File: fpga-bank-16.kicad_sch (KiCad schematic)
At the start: 3 parts, among them U4 XC7K160T-FFG676

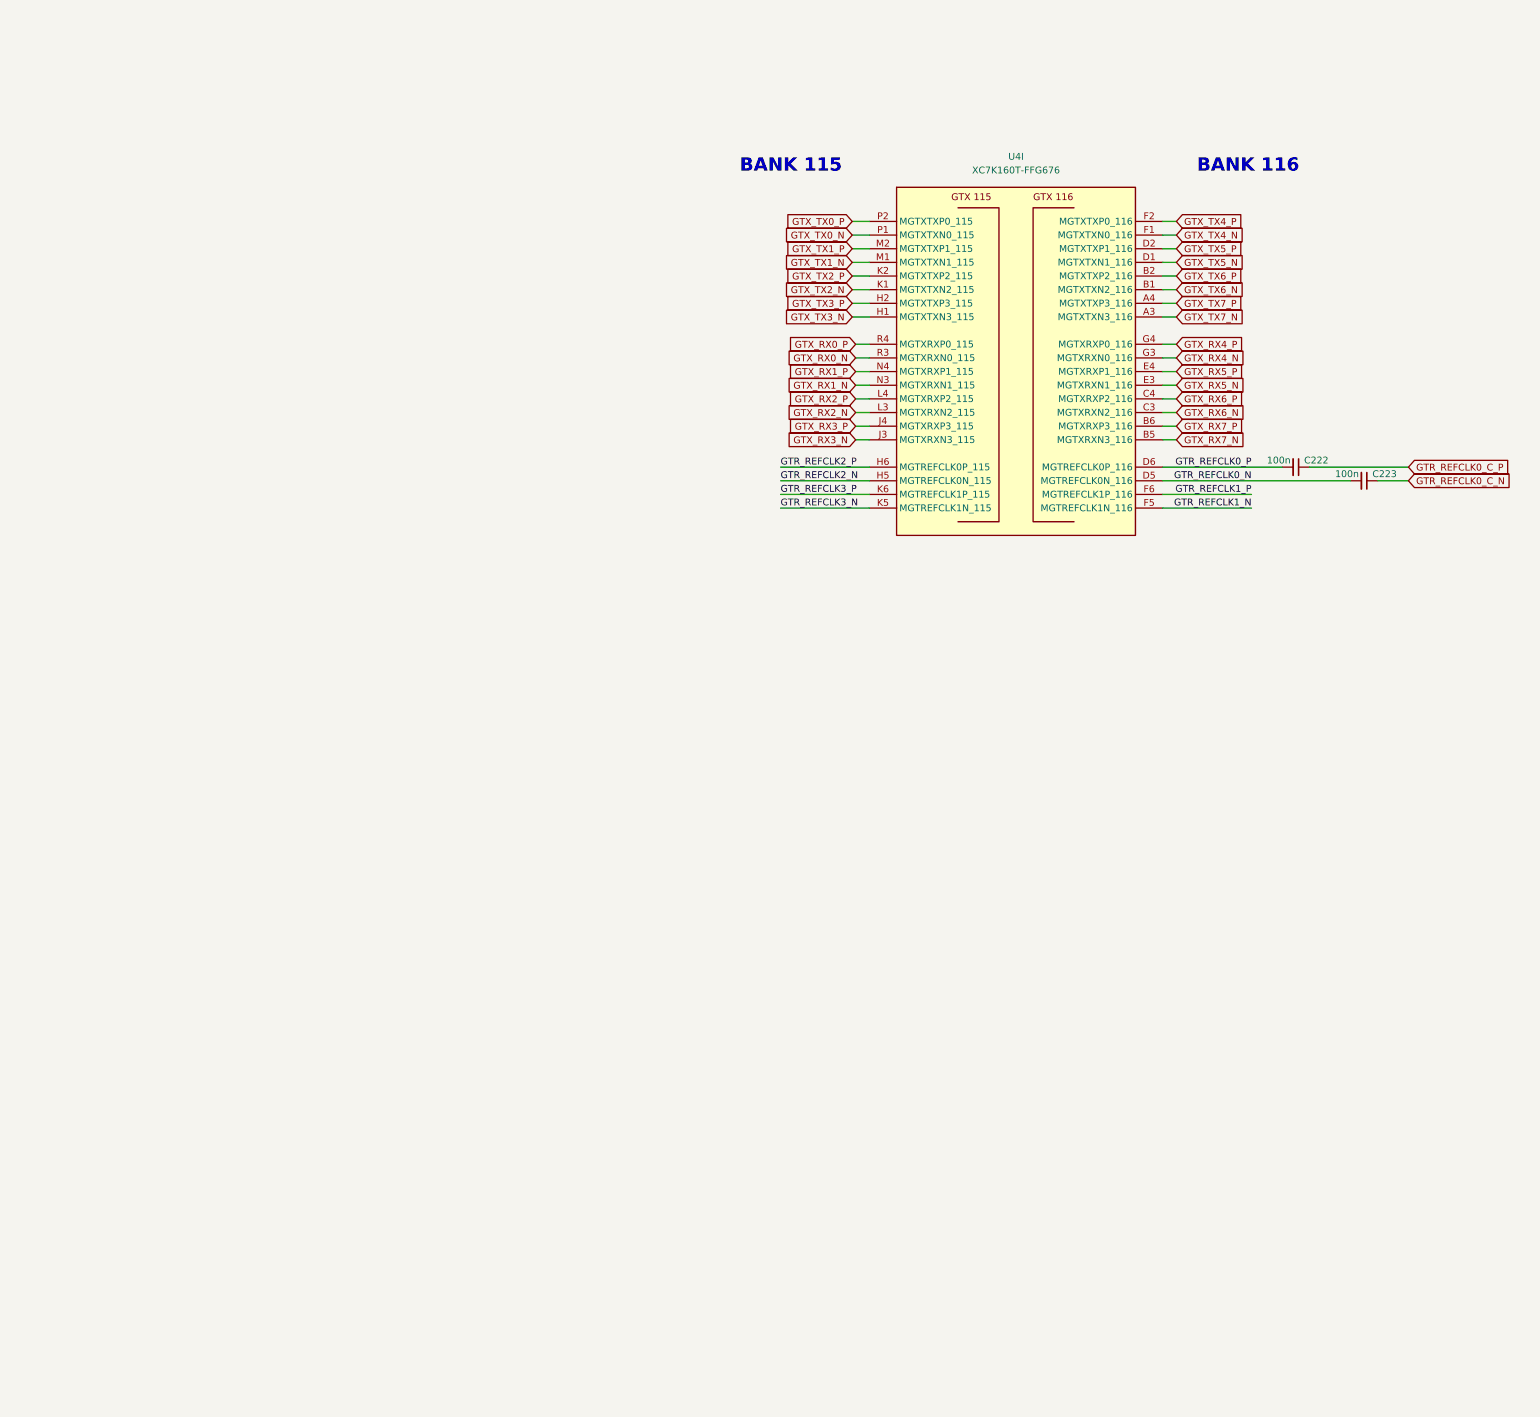
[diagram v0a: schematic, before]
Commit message: Finish creating hierarchical buses and structure, start reconnecting signals
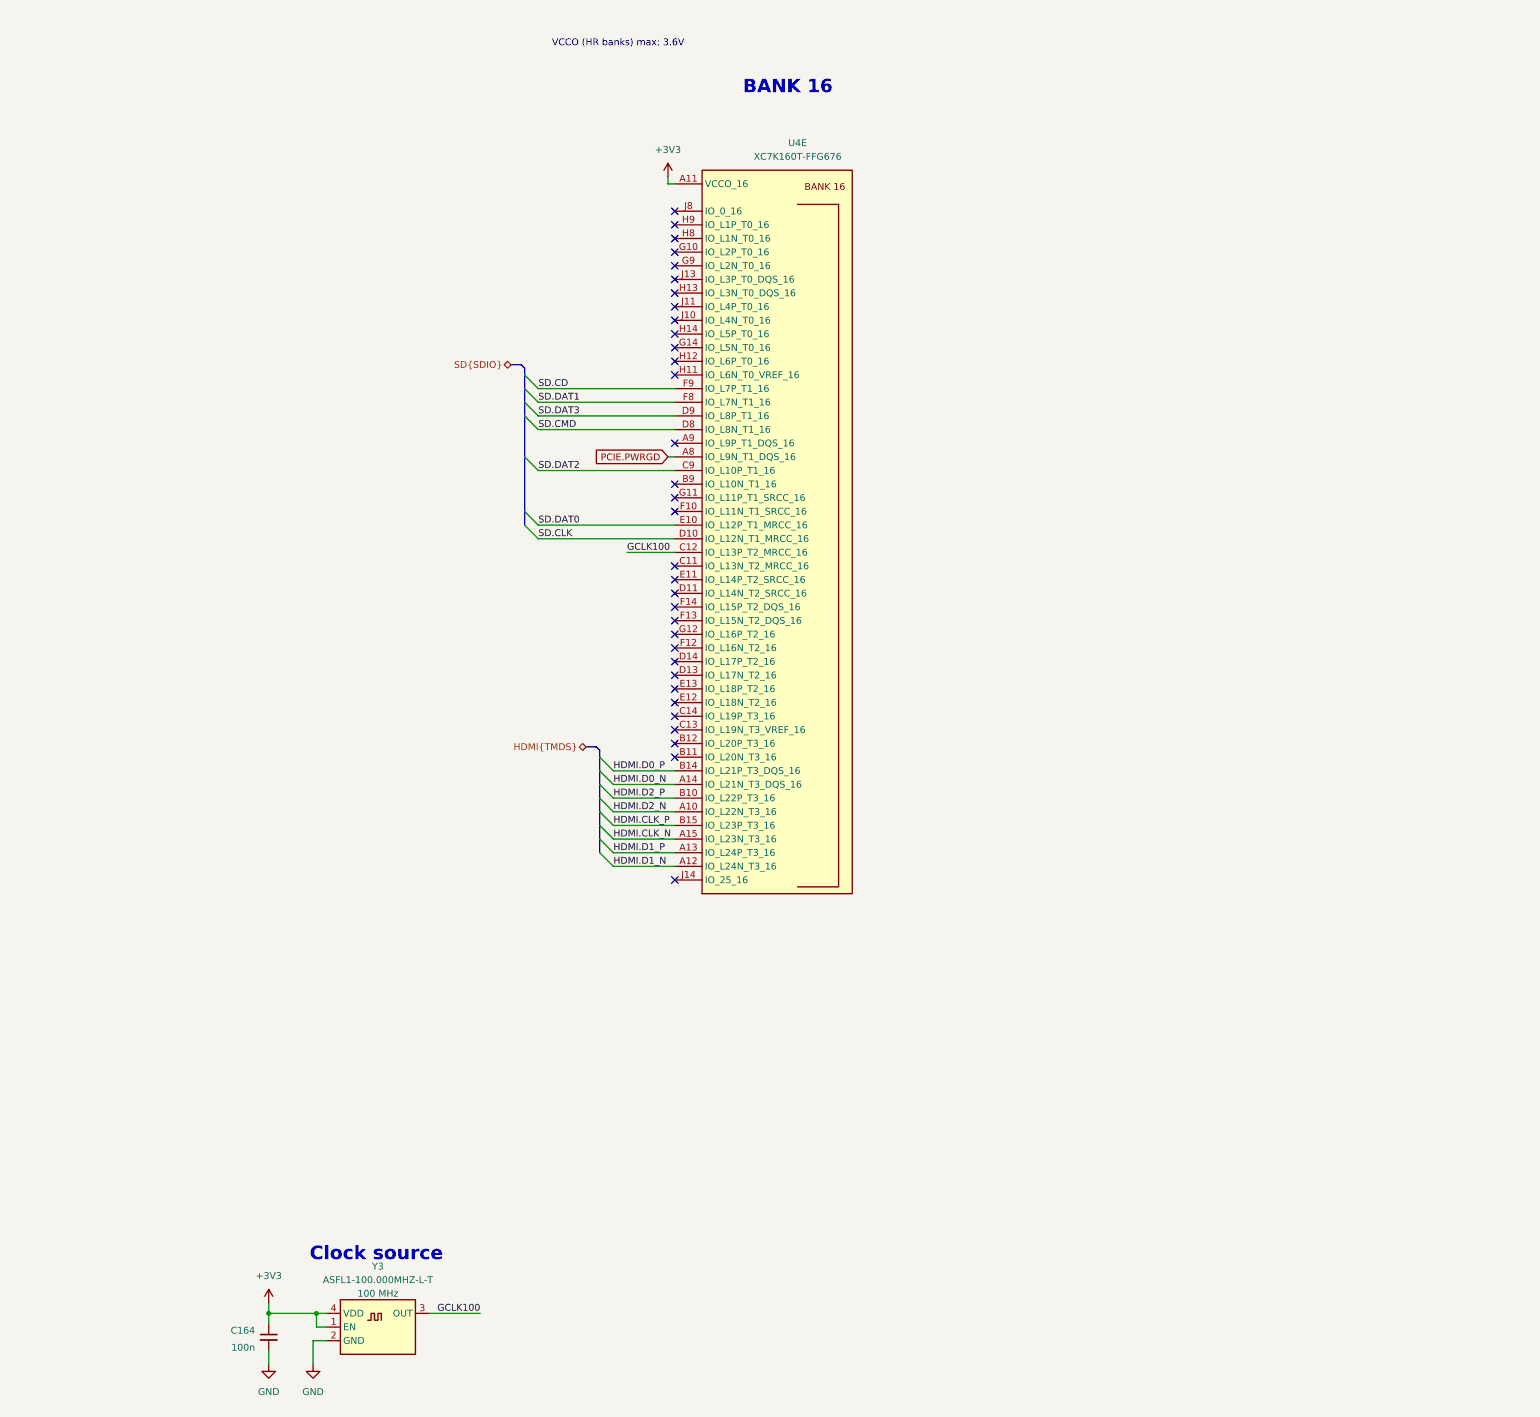
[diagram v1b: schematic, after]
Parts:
- removed C222, C223: C_100n_0402, sodimm-ddr5-tester-footprints:C_0402_1005Metric, symbol sodimm-ddr5-tester:C_100n_0402
- removed U4: XC7K160T-FFG676, sodimm-ddr5-tester-footprints:BGA-676_27x27mm_Layout26x26_P1X1mm, symbol sodimm-ddr5-tester:XC7K160T-FFG676
- added C164: C_100n_0402, sodimm-ddr5-tester-footprints:C_0402_1005Metric, symbol sodimm-ddr5-tester:C_100n_0402
- added U4: XC7K160T-FFG676, sodimm-ddr5-tester-footprints:BGA-676_27x27mm_Layout26x26_P1X1mm, symbol sodimm-ddr5-tester:XC7K160T-FFG676
- added Y3: Oscillator_100MHz_ASFL1, sodimm-ddr5-tester-footprints:Oscillator_SMD_Abracon_ASFL1-4Pin_5.0x3.2mm, symbol sodimm-ddr5-tester:Oscillator_100MHz_ASFL1
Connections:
- new net +3V3: C164.1, U4.A11 (VCCO_16), U4.B8 (VCCO_16), U4.C15 (VCCO_16), U4.D12 (VCCO_16), U4.E9 (VCCO_16), U4.G13 (VCCO_16), U4.H10 (VCCO_16), Y3.1 (EN), Y3.4 (VDD)
- new net GCLK100: U4.C12 (IO_L13P_T2_MRCC_16), Y3.3 (OUT)
- new net GND: C164.2, Y3.2 (GND)
- new net HDMI.CLK_N: U4.A15 (IO_L23N_T3_16)
- new net HDMI.CLK_P: U4.B15 (IO_L23P_T3_16)
- new net HDMI.D0_N: U4.A14 (IO_L21N_T3_DQS_16)
- new net HDMI.D0_P: U4.B14 (IO_L21P_T3_DQS_16)
- new net HDMI.D1_N: U4.A12 (IO_L24N_T3_16)
- new net HDMI.D1_P: U4.A13 (IO_L24P_T3_16)
- new net HDMI.D2_N: U4.A10 (IO_L22N_T3_16)
- new net HDMI.D2_P: U4.B10 (IO_L22P_T3_16)
- new net PCIE.PWRGD: U4.A8 (IO_L9N_T1_DQS_16)
- new net SD.CD: U4.F9 (IO_L7P_T1_16)
- new net SD.CLK: U4.D10 (IO_L12N_T1_MRCC_16)
- new net SD.CMD: U4.D8 (IO_L8N_T1_16)
- new net SD.DAT0: U4.E10 (IO_L12P_T1_MRCC_16)
- new net SD.DAT1: U4.F8 (IO_L7N_T1_16)
- new net SD.DAT2: U4.C9 (IO_L10P_T1_16)
- new net SD.DAT3: U4.D9 (IO_L8P_T1_16)
- no-connect marks 0 -> 33
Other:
- note added: "BANK 16"
- note added: "Clock source"
- note added: "VCCO (HR banks) max: 3.6V"
- note removed: "BANK 115"
- note removed: "BANK 116"

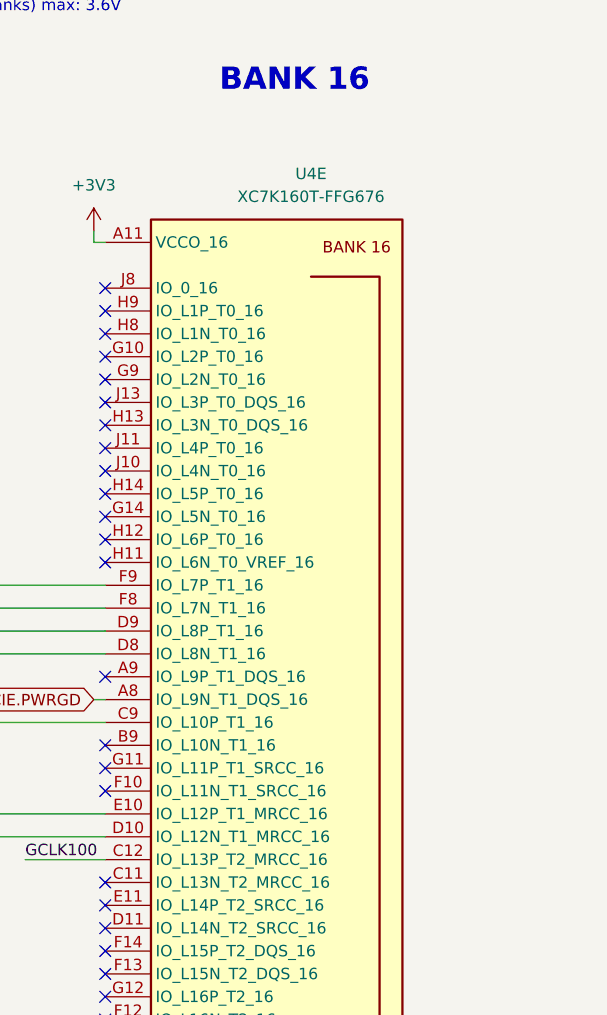
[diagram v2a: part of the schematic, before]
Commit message: Fix FPGA properties from the standardized library, update SO-DIMM symbol
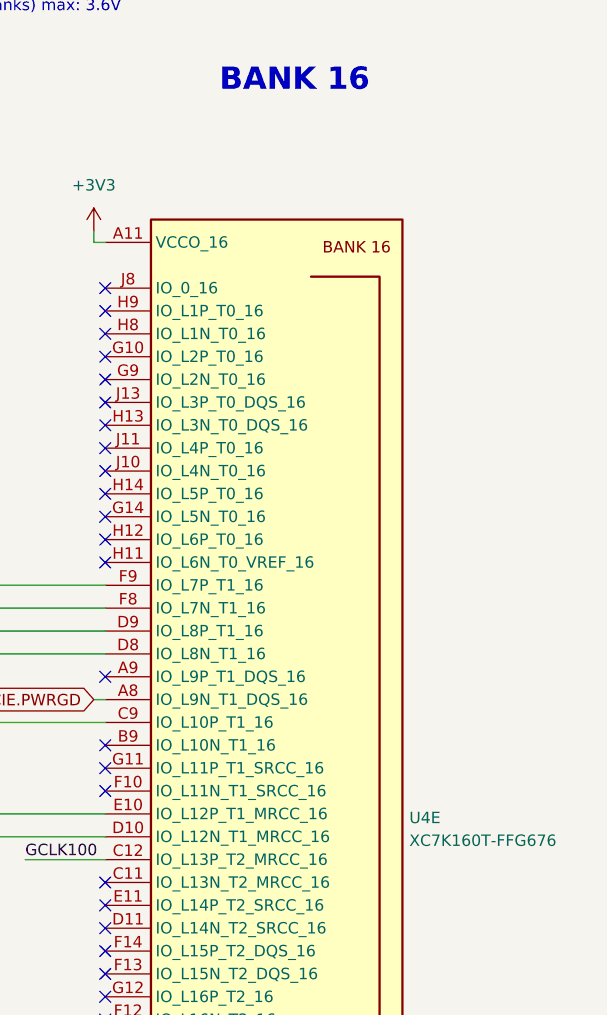
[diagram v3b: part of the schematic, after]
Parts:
- U4: footprint sodimm-ddr5-tester-footprints:BGA-676_27x27mm_Layout26x26_P1X1mm -> antmicro-footprints:BGA-676_27x27mm_Layout26x26_P1X1mm; symbol sodimm-ddr5-tester:XC7K160T-FFG676 -> antmicroMicrocontrollers:XC7K160T-FFG676; Manufacturer Xilinx -> AMD-Xilinx
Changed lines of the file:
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@@
     (pin "4")
   )
-  (symbol (lib_id "sodimm-ddr5-tester:XC7K160T-FFG676") (at 135.89 46.355 0) (unit 5)
+  (symbol (lib_id "antmicroMicrocontrollers:XC7K160T-FFG676") (at 135.89 46.355 0) (unit 5)
     (in_bom yes) (on_board yes) (fields_autoplaced)
-    (property "Reference" "U4" (id 0) (at 158.75 38.735 0))
-    (property "Value" "XC7K160T-FFG676" (id 1) (at 158.75 41.275 0)
-      (effects (font (size 1.27 1.27) (thickness 0.15)))
+    (property "Reference" "U4" (id 0) (at 169.672 110.2944 0)
+      (effects (font (size 1.27 1.27)) (justify left))
     )
-    (property "Footprint" "sodimm-ddr5-tester-footprints:BGA-676_27x27mm_Layout26x26_P1X1mm" (id 2) (at 204.47 48.895 0)
+    (property "Value" "XC7K160T-FFG676" (id 1) (at 169.672 112.8247 0)
+      (effects (font (size 1.27 1.27) (thickness 0.15)) (justify left))
+    )
+    (property "Footprint" "antmicro-footprints:BGA-676_27x27mm_Layout26x26_P1X1mm" (id 2) (at 204.47 48.895 0)
       (effects (font (size 1.27 1.27) (thickness 0.15)) (justify left bottom) hide)
     )
@@
       (effects (font (size 1.27 1.27) (thickness 0.15)) (justify left bottom) hide)
     )
-    (property "Manufacturer" "Xilinx" (id 7) (at 135.89 46.355 0)
+    (property "Manufacturer" "AMD-Xilinx" (id 7) (at 135.89 46.355 0)
       (effects (font (size 1.27 1.27)) hide)
     )

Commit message: Loclib of the project
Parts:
- U4: footprint antmicro-footprints:BGA-676_27x27mm_Layout26x26_P1X1mm -> sodimm-ddr5-tester-footprints:BGA-676_27x27mm_Layout26x26_P1X1mm; symbol antmicroMicrocontrollers:XC7K160T-FFG676 -> sodimm-ddr5-tester:XC7K160T-FFG676

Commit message: Finish schematic cleanup
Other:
- moved on the sheet: C164, U4E, Y3

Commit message: Clean schematic DRC
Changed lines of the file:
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@@
     (effects (font (size 1.27 1.27)) (justify right))
   )
-  (symbol (lib_id "sodimm-ddr5-tester:GND") (at 34.29 267.335 0) (mirror y) (unit 1)
+  (symbol (lib_id "power:GND") (at 34.29 267.335 0) (mirror y) (unit 1)
     (in_bom yes) (on_board yes) (fields_autoplaced)
     (property "Reference" "#PWR0265" (id 0) (at 34.29 273.685 0)
       (effects (font (size 1.27 1.27)) hide)
     )
-    (property "Value" "GND" (id 1) (at 34.29 272.415 0))
-    (property "Footprint" "" (id 2) (at 34.29 267.335 0)
-      (effects (font (size 1.27 1.27)) hide)
-    )
-    (property "Datasheet" "" (id 3) (at 34.29 267.335 0)
-      (effects (font (size 1.27 1.27)) hide)
+    (property "Value" "GND" (id 1) (at 25.4 272.415 0)
+      (effects (font (size 1.27 1.27) (thickness 0.15)) (justify left bottom))
+    )
+    (property "Footprint" "" (id 2) (at 25.4 274.955 0)
+      (effects (font (size 1.27 1.27) (thickness 0.15)) (justify left bottom) hide)
+    )
+    (property "Datasheet" "" (id 3) (at 25.4 280.035 0)
+      (effects (font (size 1.27 1.27) (thickness 0.15)) (justify left bottom) hide)
     )
     (property "Author" "Antmicro" (id 4) (at 25.4 274.955 0)
@@
     (pin "T6")
   )
-  (symbol (lib_id "sodimm-ddr5-tester:+3V3") (at 26.035 255.905 0) (unit 1)
+  (symbol (lib_id "power:+3V3") (at 26.035 255.905 0) (unit 1)
     (in_bom yes) (on_board yes) (fields_autoplaced)
     (property "Reference" "#PWR0263" (id 0) (at 26.035 259.715 0)
       (effects (font (size 1.27 1.27)) hide)
     )
-    (property "Value" "+3V3" (id 1) (at 26.035 250.825 0))
-    (property "Footprint" "" (id 2) (at 26.035 255.905 0)
-      (effects (font (size 1.27 1.27)) hide)
-    )
-    (property "Datasheet" "" (id 3) (at 26.035 255.905 0)
-      (effects (font (size 1.27 1.27)) hide)
+    (property "Value" "+3V3" (id 1) (at 22.86 253.365 0)
+      (effects (font (size 1.27 1.27) (thickness 0.15)) (justify left bottom))
+    )
+    (property "Footprint" "" (id 2) (at 41.275 263.525 0)
+      (effects (font (size 1.27 1.27) (thickness 0.15)) (justify left bottom) hide)
+    )
+    (property "Datasheet" "" (id 3) (at 41.275 266.065 0)
+      (effects (font (size 1.27 1.27) (thickness 0.15)) (justify left bottom) hide)
+    )
+    (property "Author" "Antmicro" (id 4) (at 41.275 258.445 0)
+      (effects (font (size 1.27 1.27) (thickness 0.15)) (justify left bottom) hide)
+    )
+    (property "License" "Apache-2.0" (id 5) (at 41.275 260.985 0)
+      (effects (font (size 1.27 1.27) (thickness 0.15)) (justify left bottom) hide)
     )
     (pin "1")
   )
-  (symbol (lib_id "sodimm-ddr5-tester:GND") (at 26.035 267.335 0) (mirror y) (unit 1)
+  (symbol (lib_id "power:GND") (at 26.035 267.335 0) (mirror y) (unit 1)
     (in_bom yes) (on_board yes) (fields_autoplaced)
     (property "Reference" "#PWR0264" (id 0) (at 26.035 273.685 0)
       (effects (font (size 1.27 1.27)) hide)
     )
-    (property "Value" "GND" (id 1) (at 26.035 272.415 0))
-    (property "Footprint" "" (id 2) (at 26.035 267.335 0)
-      (effects (font (size 1.27 1.27)) hide)
-    )
-    (property "Datasheet" "" (id 3) (at 26.035 267.335 0)
-      (effects (font (size 1.27 1.27)) hide)
+    (property "Value" "GND" (id 1) (at 17.145 272.415 0)
+      (effects (font (size 1.27 1.27) (thickness 0.15)) (justify left bottom))
+    )
+    (property "Footprint" "" (id 2) (at 17.145 274.955 0)
+      (effects (font (size 1.27 1.27) (thickness 0.15)) (justify left bottom) hide)
+    )
+    (property "Datasheet" "" (id 3) (at 17.145 280.035 0)
+      (effects (font (size 1.27 1.27) (thickness 0.15)) (justify left bottom) hide)
     )
     (property "Author" "Antmicro" (id 4) (at 17.145 274.955 0)
@@
     (pin "1")
   )
-  (symbol (lib_id "sodimm-ddr5-tester:+3V3") (at 184.15 71.12 0) (unit 1)
+  (symbol (lib_id "power:+3V3") (at 184.15 71.12 0) (unit 1)
     (in_bom yes) (on_board yes) (fields_autoplaced)
     (property "Reference" "#PWR0262" (id 0) (at 184.15 74.93 0)
       (effects (font (size 1.27 1.27)) hide)
     )
-    (property "Value" "+3V3" (id 1) (at 184.15 66.04 0))
-    (property "Footprint" "" (id 2) (at 184.15 71.12 0)
-      (effects (font (size 1.27 1.27)) hide)
-    )
-    (property "Datasheet" "" (id 3) (at 184.15 71.12 0)
-      (effects (font (size 1.27 1.27)) hide)
+    (property "Value" "+3V3" (id 1) (at 180.975 68.58 0)
+      (effects (font (size 1.27 1.27) (thickness 0.15)) (justify left bottom))
+    )
+    (property "Footprint" "" (id 2) (at 199.39 78.74 0)
+      (effects (font (size 1.27 1.27) (thickness 0.15)) (justify left bottom) hide)
+    )
+    (property "Datasheet" "" (id 3) (at 199.39 81.28 0)
+      (effects (font (size 1.27 1.27) (thickness 0.15)) (justify left bottom) hide)
+    )
+    (property "Author" "Antmicro" (id 4) (at 199.39 73.66 0)
+      (effects (font (size 1.27 1.27) (thickness 0.15)) (justify left bottom) hide)
+    )
+    (property "License" "Apache-2.0" (id 5) (at 199.39 76.2 0)
+      (effects (font (size 1.27 1.27) (thickness 0.15)) (justify left bottom) hide)
     )
     (pin "1")
